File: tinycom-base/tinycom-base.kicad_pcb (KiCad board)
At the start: 2 copper layers, 45.2 x 45.2 mm, 13 parts, among them J1 MICRO_SD_HINGE, P1 CONN_02X08, P2 CONN_02X08, P3 USB_A, P4 CONN_01X12, P5 CONN_02X12, U1 OLIMEX_IC_AXP209, U2 STM32-48PIN, U3 fpc_24

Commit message: add base
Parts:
- removed P5: CONN_02X12, Pin_Headers:Pin_Header_Straight_2x12
- removed U2: STM32-48PIN, mods:QFP50P900X900X160-48N
- removed U3: fpc_24, tinycom:fpc_24
- P4: value CONN_01X12 -> USB_B; footprint Pin_Headers:Pin_Header_Straight_1x12 -> Connect:USB_Micro-B
- moved P4 14.7 mm to (128.3, 102.1), turned to 270 degrees
- moved U1 2.65 mm to (141.9, 102.5)
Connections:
- P4 pad 6: Net-(P4-Pad6) -> (no net)

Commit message: xxx
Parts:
- U1: footprint ax209:ax209-OLIMEX_IC_QFN48 -> tinycom:ax209-OLIMEX_IC_QFN48
- moved J1 43.6 mm to (124.5, 107.8), turned to 270 degrees
- moved P4 8.95 mm to (128.4, 93.2)
- moved U1 2.75 mm to (143.3, 100.1)

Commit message: prepare base
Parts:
- added C1: C_Small, Capacitors_SMD:C_0805, F.Cu at (140.5, 91.9)
- added C10: C_Small, Capacitors_SMD:C_0805, F.Cu at (133.6, 90.2)
- added C11: CP_Small, Capacitors_Elko_ThroughHole:Elko_vert_11.2x6.3mm_RM2.5_CopperClear, F.Cu at (164.7, 112.3)
- added C12: CP_Small, Capacitors_Elko_ThroughHole:Elko_vert_11.2x6.3mm_RM2.5_CopperClear, F.Cu at (135.0, 93.5)
- added C13: C_Small, Capacitors_SMD:C_0805, F.Cu at (140.0, 105.4)
- added C2: C_Small, Capacitors_SMD:C_0805, F.Cu at (151.8, 91.8)
- added C3: C_Small, Capacitors_SMD:C_0805, F.Cu at (140.3, 101.7)
- added C4: C_Small, Capacitors_SMD:C_0805, F.Cu at (141.0, 110.7)
- added C5: C_Small, Capacitors_SMD:C_0805, F.Cu at (151.4, 110.7)
- added C6: C_Small, Capacitors_SMD:C_0805, F.Cu at (150.9, 101.7)
- added C7: C_Small, Capacitors_SMD:C_0805, F.Cu at (163.6, 90.0)
- added C8: C_Small, Capacitors_SMD:C_0805, F.Cu at (139.9, 107.4)
- added C9: C_Small, Capacitors_SMD:C_0805, F.Cu at (155.7, 109.2)
- added D1: D_Schottky_Small, Diodes_SMD:SMA_Standard, F.Cu at (156.6, 89.4)
- added L1: SMD-INDUCTOR-2.2UH-20%-1.2A(0805), cd32:CD32, F.Cu at (148.3, 89.8)
- added L2: SMD-INDUCTOR-2.2UH-20%-1.2A(0805), cd32:CD32, F.Cu at (147.8, 99.6)
- added L3: SMD-INDUCTOR-2.2UH-20%-1.2A(0805), cd32:CD32, F.Cu at (148.3, 108.8)
- added R1: R_Small, Resistors_SMD:R_0805, F.Cu at (149.5, 93.6)
- added R10: R_Small, Resistors_SMD:R_0805, B.Cu at (130.4, 106.7)
- added R11: R_Small, Resistors_SMD:R_0805, B.Cu at (130.4, 104.6)
- added R12: R_Small, Resistors_SMD:R_0805, B.Cu at (130.4, 102.6)
- added R2: R_Small, Resistors_SMD:R_0805, F.Cu at (147.2, 93.6)
- added R3: R_Small, Resistors_SMD:R_0805, F.Cu at (149.4, 112.7)
- added R4: R_Small, Resistors_SMD:R_0805, F.Cu at (147.3, 112.7)
- added R5: R_Small, Resistors_SMD:R_0805, F.Cu at (148.8, 103.4)
- added R6: R_Small, Resistors_SMD:R_0805, F.Cu at (146.8, 103.4)
- added R7: R_Small, Resistors_SMD:R_0805, F.Cu at (161.4, 90.0)
- added R8: R_Small, Resistors_SMD:R_0805, B.Cu at (130.4, 111.6)
- added R9: R_Small, Resistors_SMD:R_0805, B.Cu at (130.4, 109.6)
- added U2: SY8008BAAC, opendous:SOT23-5_Opendous, F.Cu at (143.8, 101.7)
- added U3: SY8008BAAC, opendous:SOT23-5_Opendous, F.Cu at (144.3, 110.6)
- J1: moved to F.Cu
- U1: value OLIMEX_IC_AXP209 -> SY8008BAAC; footprint tinycom:ax209-OLIMEX_IC_QFN48 -> opendous:SOT23-5_Opendous
- moved U1 8.28 mm to (143.9, 91.8), turned to 90 degrees
- moved J1 0.56 mm to (124.5, 107.3), turned to 90 degrees
- moved P2 0.49 mm to (155.8, 85.5)
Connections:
- net Net-(P1-Pad1) renamed UART1_TX
- net Net-(P1-Pad3) renamed UART1_RX
- J1 pad 1: Net-(J1-Pad1) -> SDC0_D2
- J1 pad 10: Net-(J1-Pad10) -> GND
- J1 pad 11: Net-(J1-Pad11) -> GND
- J1 pad 12: Net-(J1-Pad12) -> GND
- J1 pad 2: Net-(J1-Pad2) -> SDC0_D3
- J1 pad 3: Net-(J1-Pad3) -> SDC0_CMD
- J1 pad 4: Net-(J1-Pad4) -> VCC_33
- J1 pad 5: Net-(J1-Pad5) -> SDC0_CLK
- J1 pad 6: Net-(J1-Pad6) -> GND
- J1 pad 7: Net-(J1-Pad7) -> SDC0_D0
- J1 pad 8: Net-(J1-Pad8) -> SDC0_D1
- J1 pad 9: Net-(J1-Pad9) -> GND
- P1 pad 10: Net-(P1-Pad10) -> UDP1
- P1 pad 11: Net-(P1-Pad11) -> SDC0_CMD
- P1 pad 12: Net-(P1-Pad12) -> UDM1
- P1 pad 13: Net-(P1-Pad13) -> SDC0_D3
- P1 pad 14: Net-(P1-Pad14) -> UDP0
- P1 pad 15: Net-(P1-Pad15) -> SDC0_D2
- P1 pad 16: Net-(P1-Pad16) -> UDM0
- P1 pad 2: Net-(P1-Pad2) -> GND
- P1 pad 4: Net-(P1-Pad4) -> VCC_15
- P1 pad 5: Net-(P1-Pad5) -> SDC0_D1
- P1 pad 6: Net-(P1-Pad6) -> VCC_14
- P1 pad 7: Net-(P1-Pad7) -> SDC0_D0
- P1 pad 8: Net-(P1-Pad8) -> VCC_33
- P1 pad 9: Net-(P1-Pad9) -> SDC0_CLK
- P2 pad 2: Net-(P2-Pad2) -> GND
- P2 pad 4: Net-(P2-Pad4) -> VCC_30
- P3 pad 1: Net-(P3-Pad1) -> +5V
- P3 pad 2: Net-(P3-Pad2) -> UDM1
- P3 pad 3: Net-(P3-Pad3) -> UDP1
- P3 pad 4: Net-(P3-Pad4) -> GND
- P4 pad 1: Net-(P4-Pad1) -> +5V
- P4 pad 2: Net-(P4-Pad2) -> UDM0
- P4 pad 3: Net-(P4-Pad3) -> UDP0
- P4 pad 4: Net-(P4-Pad4) -> GND
- P4 pad 5: Net-(P4-Pad5) -> GND
- U1 pad 1: Net-(U1-Pad1) -> +5V
- U1 pad 2: Net-(U1-Pad2) -> GND
- U1 pad 4: Net-(U1-Pad4) -> +5V
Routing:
- net VCC_33: track 0.00 -> 103.6 mm, vias 0 -> 1
- net +5V: track 0.00 -> 82.2 mm, vias 0 -> 2
- net GND: track 0.00 -> 50.0 mm, vias 0 -> 17
- net VCC_14: track 0.00 -> 48.7 mm
- net UDP0: track 0.00 -> 45.8 mm, vias 0 -> 1
- net UDM0: track 0.00 -> 44.7 mm, vias 0 -> 1
- net UDP1: track 0.00 -> 36.4 mm, vias 0 -> 1
- net SDC0_D2: track 0.00 -> 30.9 mm, vias 0 -> 2
- net UDM1: track 0.00 -> 30.8 mm, vias 0 -> 1
- net SDC0_D3: track 0.00 -> 27.4 mm, vias 0 -> 2
- net VCC_15: track 0.00 -> 26.0 mm
- net SDC0_CMD: track 0.00 -> 24.3 mm, vias 0 -> 2
- net SDC0_CLK: track 0.00 -> 18.1 mm, vias 0 -> 1
- net SDC0_D0: track 0.00 -> 17.6 mm, vias 0 -> 2
- net VCC_30: track 0.00 -> 16.3 mm
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- added copper zone on B.Cu, net GND
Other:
- net class Default: via_drill 0.4 -> 0.3
- rule pad_to_mask_clearance: 0.2 -> 0.07
- board text added: "TinyCom"
- board text added: "http://tinycom.org/"

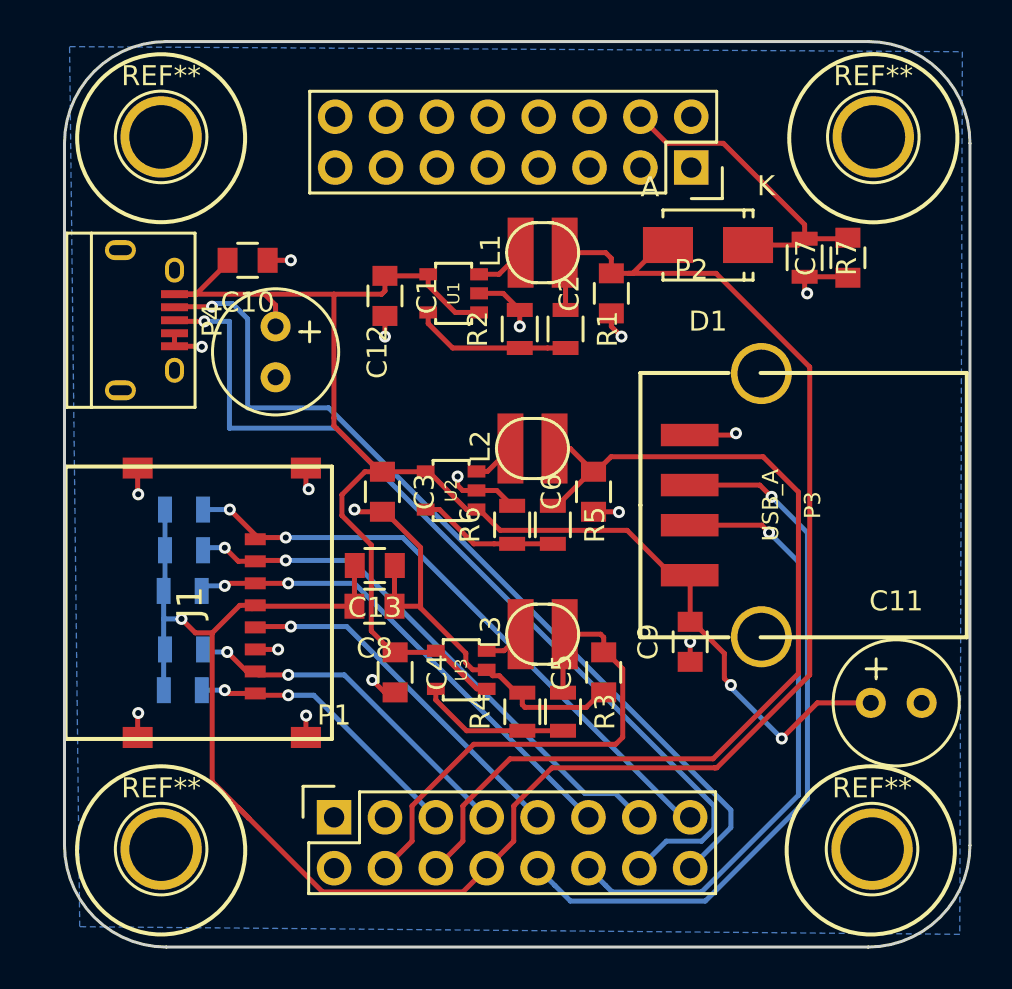
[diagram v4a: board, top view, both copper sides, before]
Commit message: ddr data routing
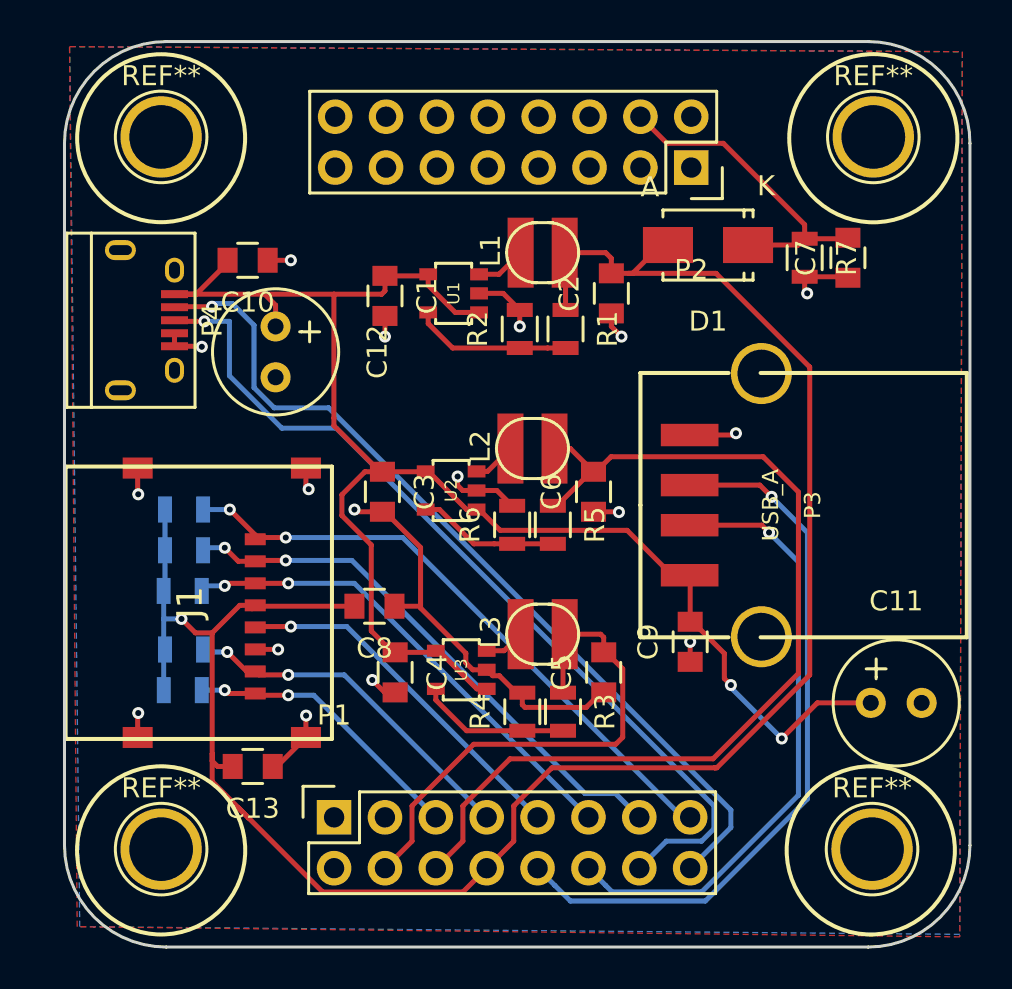
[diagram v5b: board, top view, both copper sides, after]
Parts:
- moved C13 11.7 mm to (133.9, 115.4)
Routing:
- net UDP0: track 45.8 -> 44.3 mm
- net UDM0: track 44.7 -> 43.9 mm
- net VCC_33: track 103.6 -> 103.0 mm
- added copper zone on F.Cu, net GND
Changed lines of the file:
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@@
   (general
     (links 89)
-    (no_connects 6)
+    (no_connects 4)
     (area 122.46646 73.647334 169.818661 124.580666)
     (thickness 1.6)
     (drawings 14)
-    (tracks 324)
+    (tracks 328)
     (zones 0)
     (modules 41)
@@
     (visible_elements FFFFFF7F)
     (pcbplotparams
-      (layerselection 0x00030_80000001)
+      (layerselection 0x010f0_80000001)
       (usegerberextensions false)
       (excludeedgelayer true)
@@
       (drillshape 0)
       (scaleselection 1)
-      (outputdirectory ""))
+      (outputdirectory gerber/))
   )
   (net 0 "")
@@
   )
   (module Capacitors_SMD:C_0805 (layer F.Cu)
-    (at 139.954 105.41 180)
+    (at 133.858 115.443 180)
     (descr "Capacitor SMD 0805, reflow soldering, AVX (see smccp.pdf)")
     (tags "capacitor 0805")
@@
   (segment (start 140.462 90.948) (end 142.5415 90.948) (width 0.25) (layer F.Cu) (net 15))
   (segment (start 142.5415 90.948) (end 142.621 90.8685) (width 0.25) (layer F.Cu) (net 15))
-  (segment (start 140.938 107.442) (end 140.938 105.426) (width 0.25) (layer F.Cu) (net 16))
-  (segment (start 140.938 105.426) (end 140.954 105.41) (width 0.25) (layer F.Cu) (net 16))
+  (segment (start 134.858 115.443) (end 135.06704 115.443) (width 0.25) (layer F.Cu) (net 16))
+  (segment (start 135.06704 115.443) (end 136.51484 113.9952) (width 0.25) (layer F.Cu) (net 16))
   (segment (start 140.97 111.744) (end 140.446 111.744) (width 0.25) (layer F.Cu) (net 16))
   (segment (start 140.446 111.744) (end 139.827 111.125) (width 0.25) (layer F.Cu) (net 16))
@@
   (segment (start 148.928 99.568) (end 149.717 99.568) (width 0.25) (layer F.Cu) (net 26))
   (segment (start 149.717 99.568) (end 150.876 100.727) (width 0.25) (layer F.Cu) (net 26))
-  (segment (start 138.938 107.442) (end 138.938 105.426) (width 0.25) (layer F.Cu) (net 27))
-  (segment (start 138.938 105.426) (end 138.954 105.41) (width 0.25) (layer F.Cu) (net 27))
+  (segment (start 131.835999 108.773311) (end 131.835999 114.807136) (width 0.25) (layer F.Cu) (net 27))
+  (segment (start 131.835999 114.807136) (end 131.835999 116.196129) (width 0.25) (layer F.Cu) (net 27))
+  (segment (start 132.858 115.443) (end 132.108 115.443) (width 0.25) (layer F.Cu) (net 27))
+  (segment (start 132.108 115.443) (end 131.835999 115.170999) (width 0.25) (layer F.Cu) (net 27))
+  (segment (start 131.835999 115.170999) (end 131.835999 114.807136) (width 0.25) (layer F.Cu) (net 27))
   (segment (start 148.793859 115.512011) (end 156.93547 115.512011) (width 0.25) (layer F.Cu) (net 27))
   (segment (start 152.64 90.821) (end 156.991482 90.821) (width 0.25) (layer F.Cu) (net 27))
@@
   (segment (start 133.985 107.39882) (end 133.21049 107.39882) (width 0.25) (layer F.Cu) (net 27))
   (segment (start 133.21049 107.39882) (end 131.835999 108.773311) (width 0.25) (layer F.Cu) (net 27))
-  (segment (start 131.835999 108.773311) (end 131.835999 116.196129) (width 0.25) (layer F.Cu) (net 27))
   (segment (start 131.835999 116.196129) (end 133.662371 118.022501) (width 0.25) (layer F.Cu) (net 27))
   (segment (start 129.413 111.628) (end 129.418 111.633) (width 0.25) (layer B.Cu) (net 27))
@@
   (segment (start 159.27578 103.39578) (end 159.639 103.759) (width 0.25) (layer F.Cu) (net 29))
   (via (at 159.639 103.759) (size 0.6) (drill 0.3) (layers F.Cu B.Cu) (net 29))
+  (segment (start 132.69613 93.218) (end 132.69613 95.935386) (width 0.25) (layer B.Cu) (net 30))
+  (segment (start 132.69613 95.935386) (end 135.312744 98.552) (width 0.25) (layer B.Cu) (net 30))
+  (segment (start 135.312744 98.552) (end 138.03013 98.552) (width 0.25) (layer B.Cu) (net 30))
   (segment (start 153.162 120.523) (end 154.513399 119.171601) (width 0.25) (layer B.Cu) (net 30))
   (segment (start 154.513399 119.171601) (end 156.272529 119.171601) (width 0.25) (layer B.Cu) (net 30))
@@
   (segment (start 156.890601 118.553529) (end 156.890601 117.412471) (width 0.25) (layer B.Cu) (net 30))
   (segment (start 156.890601 117.412471) (end 138.03013 98.552) (width 0.25) (layer B.Cu) (net 30))
-  (segment (start 132.69613 98.552) (end 132.69613 93.218) (width 0.25) (layer B.Cu) (net 30))
-  (segment (start 138.03013 98.552) (end 132.69613 98.552) (width 0.25) (layer B.Cu) (net 30))
   (segment (start 132.69613 93.218) (end 131.445 93.218) (width 0.25) (layer B.Cu) (net 30))
   (segment (start 131.445 93.218) (end 130.01 93.218) (width 0.25) (layer F.Cu) (net 30))
   (segment (start 130.01 93.218) (end 129.954 93.162) (width 0.25) (layer F.Cu) (net 30))
   (via (at 131.445 93.218) (size 0.6) (drill 0.3) (layers F.Cu B.Cu) (net 30))
-  (segment (start 155.702 120.523) (end 157.734 118.491) (width 0.25) (layer B.Cu) (net 31))
-  (segment (start 157.734 118.491) (end 157.734 117.61946) (width 0.25) (layer B.Cu) (net 31))
-  (segment (start 132.842 92.329) (end 131.98401 92.329) (width 0.25) (layer B.Cu) (net 31))
-  (segment (start 131.98401 92.329) (end 131.826 92.48701) (width 0.25) (layer B.Cu) (net 31))
-  (segment (start 157.734 117.61946) (end 137.65054 97.536) (width 0.25) (layer B.Cu) (net 31))
-  (segment (start 137.65054 97.536) (end 133.604 97.536) (width 0.25) (layer B.Cu) (net 31))
-  (segment (start 133.604 97.536) (end 133.604 93.091) (width 0.25) (layer B.Cu) (net 31))
-  (segment (start 133.604 93.091) (end 132.842 92.329) (width 0.25) (layer B.Cu) (net 31))
+  (segment (start 131.826 92.48701) (end 131.98401 92.329) (width 0.25) (layer B.Cu) (net 31))
+  (segment (start 131.98401 92.329) (end 132.842 92.329) (width 0.25) (layer B.Cu) (net 31))
+  (segment (start 133.925429 96.528275) (end 134.933154 97.536) (width 0.25) (layer B.Cu) (net 31))
+  (segment (start 132.842 92.329) (end 133.925429 93.412429) (width 0.25) (layer B.Cu) (net 31))
+  (segment (start 133.925429 93.412429) (end 133.925429 96.528275) (width 0.25) (layer B.Cu) (net 31))
+  (segment (start 134.933154 97.536) (end 137.65054 97.536) (width 0.25) (layer B.Cu) (net 31))
+  (segment (start 137.65054 97.536) (end 157.734 117.61946) (width 0.25) (layer B.Cu) (net 31))
+  (segment (start 157.734 117.61946) (end 157.734 118.491) (width 0.25) (layer B.Cu) (net 31))
+  (segment (start 157.734 118.491) (end 155.702 120.523) (width 0.25) (layer B.Cu) (net 31))
   (segment (start 131.826 92.48701) (end 129.97899 92.48701) (width 0.25) (layer F.Cu) (net 31))
   (segment (start 129.97899 92.48701) (end 129.954 92.512) (width 0.25) (layer F.Cu) (net 31))
@@
       )
     )
+  )
+  (zone (net 16) (net_name GND) (layer F.Cu) (hatch edge 0.508)
+    (connect_pads (clearance 0.508))
+    (min_thickness 0.254)
+    (fill yes (arc_segments 16) (thermal_gap 0.508) (thermal_bridge_width 0.508))
+    (polygon
+      (pts
+        (xy 124.714 79.502) (xy 169.291 79.756) (xy 169.164 123.952) (xy 125.095 123.444)
+      )
+    )

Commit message: update base board
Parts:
- removed C10, C13, C9: C_Small, Capacitors_SMD:C_0805
- C1, C2, C3, C4, C5, C6, C7: footprint Capacitors_SMD:C_0805 -> Capacitors_SMD:C_1206
- C11, C12: footprint Capacitors_Elko_ThroughHole:Elko_vert_11.2x6.3mm_RM2.5_CopperClear -> Capacitors_Tantalum_SMD:TantalC_SizeA_EIA-3216_Reflow
- J1: footprint armory:MICRO_SD_HINGE_AMP -> tinycom:tc-MICRO_SD_HINGE_AMP
- P3: footprint opendous:USB-A-Receptacle-FCI_87583 -> tinycom:tc-con-usb-USB-A-H
- P4: footprint Connect:USB_Micro-B -> tinycom:tc-USB_Micro-B
- moved R8 4.04 mm to (132.9, 108.5)
- moved R9 3.96 mm to (132.9, 106.5)
- moved C11 3.69 mm to (161.2, 111.1)
- moved R10 3.32 mm to (132.9, 104.5)
- moved R11 3.26 mm to (132.9, 102.5)
- moved R12 3.26 mm to (132.9, 100.5)
- moved P3 2.71 mm to (159.3, 100.8), turned to 180 degrees
- moved C6 2.60 mm to (153.4, 101.3)
- moved C5 2.41 mm to (153.7, 111.2)
- moved C3 2.32 mm to (142.6, 101.5)
- moved L2 2.32 mm to (150.1, 99.3)
- moved R5 2.32 mm to (151.2, 103.1)
- moved R6 2.32 mm to (149.1, 103.1)
- moved U2 2.32 mm to (146.1, 101.4)
- moved C4 2.03 mm to (143.0, 111.2)
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- renumbered REF** to H1, REF** to H2, REF** to H3, REF** to H4
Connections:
- P1 pad 1: UART1_TX -> (no net)
- P1 pad 3: UART1_RX -> (no net)
- P2 pad 1: Net-(P2-Pad1) -> (no net)
- P2 pad 10: Net-(P2-Pad10) -> (no net)
- P2 pad 11: Net-(P2-Pad11) -> (no net)
- P2 pad 12: Net-(P2-Pad12) -> (no net)
- P2 pad 13: Net-(P2-Pad13) -> (no net)
- P2 pad 14: Net-(P2-Pad14) -> (no net)
- P2 pad 15: Net-(P2-Pad15) -> (no net)
- P2 pad 16: Net-(P2-Pad16) -> (no net)
- P2 pad 3: Net-(P2-Pad3) -> (no net)
- P2 pad 5: Net-(P2-Pad5) -> (no net)
- P2 pad 6: Net-(P2-Pad6) -> (no net)
- P2 pad 7: Net-(P2-Pad7) -> (no net)
- P2 pad 8: Net-(P2-Pad8) -> (no net)
- P2 pad 9: Net-(P2-Pad9) -> (no net)
- P4 pad 5: GND -> (no net)
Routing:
- net VCC_33: track 103.0 -> 0.00 mm, vias 1 -> 0
- net +5V: track 82.2 -> 0.00 mm, vias 2 -> 0
- net GND: track 50.2 -> 0.00 mm, vias 17 -> 0
- net VCC_14: track 48.7 -> 0.00 mm
- net UDP0: track 44.3 -> 0.00 mm, vias 1 -> 0
- net UDM0: track 43.9 -> 0.00 mm, vias 1 -> 0
- net UDP1: track 36.4 -> 0.00 mm, vias 1 -> 0
- net SDC0_D2: track 30.9 -> 0.00 mm, vias 2 -> 0
- net UDM1: track 30.8 -> 0.00 mm, vias 1 -> 0
- net SDC0_D3: track 27.4 -> 0.00 mm, vias 2 -> 0
- net VCC_15: track 26.0 -> 0.00 mm
- net SDC0_CMD: track 24.3 -> 0.00 mm, vias 2 -> 0
- net SDC0_CLK: track 18.1 -> 0.00 mm, vias 1 -> 0
- net SDC0_D0: track 17.6 -> 0.00 mm, vias 2 -> 0
- net VCC_30: track 16.3 -> 0.00 mm
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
